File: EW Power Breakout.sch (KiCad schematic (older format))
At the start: 0 parts

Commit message: Jacks and labels
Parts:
- added J1, J2, J4, J5: JACK_2P, symbol JACK_2P
- added J3: CONN_02X08, symbol CONN_02X08
- added J6: CONN_01X14, symbol CONN_01X14
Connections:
- new net +12V: J6.11 (P11)
- new net +5V: J6.13 (P13)
- new net -12V: J6.12 (P12)
- new net CV: J3.4 (P4), J6.10 (P10)
- new net GATE: J3.2 (P2), J6.9 (P9)
- new net GND: J1.3, J2.3, J4.3, J5.3, J6.14 (P14)
- new net J1: J1.1, J6.1 (P1)
- new net J1SW: J1.2, J6.2 (P2)
- new net J2: J2.1, J6.3 (P3)
- new net J2SW: J2.2, J6.4 (P4)
- new net J3: J4.1, J6.5 (P5)
- new net J3SW: J4.2, J6.6 (P6)
- new net J4: J5.1, J6.7 (P7)
- new net J4SW: J5.2, J6.8 (P8)
- no-connect marks 0 -> 1
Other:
- note added: "+12V"
- note added: "-12V"
- note added: "5V (not connected)"
- note added: "GND"
- note added: "SW=switch"
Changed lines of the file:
@@
 Comment4 ""
 $EndDescr
+$Comp
+L CONN_02X08 J3
+U 1 1 599C453D
+P 2900 3150
+F 0 "J3" H 2900 3600 50  0000 C CNN
+F 1 "CONN_02X08" V 2900 3150 50  0000 C CNN
+F 2 "" H 2900 1950 50  0001 C CNN
+F 3 "" H 2900 1950 50  0001 C CNN
+	1    2900 3150
+	1    0    0    -1
+$EndComp
+$Comp
+L CONN_01X14 J6
+U 1 1 599C456D
+P 7700 3250
+F 0 "J6" H 7700 4000 50  0000 C CNN
+F 1 "CONN_01X14" V 7800 3250 50  0000 C CNN
+F 2 "" H 7700 3250 50  0001 C CNN
+F 3 "" H 7700 3250 50  0001 C CNN
+	1    7700 3250
+	1    0    0    -1
+$EndComp
+$Comp
+L JACK_2P J1
+U 1 1 599C45B8
+P 2150 1200
+F 0 "J1" H 1800 1000 50  0000 C CNN
+F 1 "JACK_2P" H 2000 1450 50  0000 C CNN
+F 2 "" H 2150 1200 50  0001 C CNN
+F 3 "" H 2150 1200 50  0001 C CNN
+	1    2150 1200
+	1    0    0    -1
+$EndComp
+$Comp
+L JACK_2P J2
+U 1 1 599C461E
+P 2150 1750
+F 0 "J2" H 1800 1550 50  0000 C CNN
+F 1 "JACK_2P" H 2000 2000 50  0000 C CNN
+F 2 "" H 2150 1750 50  0001 C CNN
+F 3 "" H 2150 1750 50  0001 C CNN
+	1    2150 1750
+	1    0    0    -1
+$EndComp
+$Comp
+L JACK_2P J4
+U 1 1 599C4645
+P 3750 1150
+F 0 "J4" H 3400 950 50  0000 C CNN
+F 1 "JACK_2P" H 3600 1400 50  0000 C CNN
+F 2 "" H 3750 1150 50  0001 C CNN
+F 3 "" H 3750 1150 50  0001 C CNN
+	1    3750 1150
+	-1   0    0    1
+$EndComp
+$Comp
+L JACK_2P J5
+U 1 1 599C4690
+P 3750 1700
+F 0 "J5" H 3400 1500 50  0000 C CNN
+F 1 "JACK_2P" H 3600 1950 50  0000 C CNN
+F 2 "" H 3750 1700 50  0001 C CNN
+F 3 "" H 3750 1700 50  0001 C CNN
+	1    3750 1700
+	-1   0    0    1
+$EndComp
+Wire Wire Line
+	2950 1050 2950 2100
+Wire Wire Line
+	3300 1850 2950 1850
+Connection ~ 2950 1850
+Connection ~ 2950 1600
+Wire Wire Line
+	3300 1300 2950 1300
+Connection ~ 2950 1300
+Wire Wire Line
+	2950 1050 2600 1050
+Wire Wire Line
+	2950 1600 2600 1600
+$Comp
+L GND #PWR01
+U 1 1 599C47FD
+P 2950 2100
+F 0 "#PWR01" H 2950 1850 50  0001 C CNN
+F 1 "GND" H 2950 1950 50  0000 C CNN
+F 2 "" H 2950 2100 50  0001 C CNN
+F 3 "" H 2950 2100 50  0001 C CNN
+	1    2950 2100
+	1    0    0    -1
+$EndComp
+Text Label 7500 2600 2    60   ~ 0
+J1
+Text Label 7500 2700 2    60   ~ 0
+J1SW
+Text Label 2600 1300 0    60   ~ 0
+J1
+Text Label 2600 1200 0    60   ~ 0
+J1SW
+Text Label 7500 2800 2    60   ~ 0
+J2
+Text Label 7500 2900 2    60   ~ 0
+J2SW
+Text Notes 7800 2700 0    60   ~ 0
+SW=switch
+Text Label 7500 3000 2    60   ~ 0
+J3
+Text Label 7500 3100 2    60   ~ 0
+J3SW
+Text Label 7500 3200 2    60   ~ 0
+J4
+Text Label 7500 3300 2    60   ~ 0
+J4SW
+Text Label 7500 3400 2    60   ~ 0
+GATE
+Text Label 7500 3500 2    60   ~ 0
+CV
+Text Label 7500 3600 2    60   ~ 0
++12V
+Text Label 7500 3700 2    60   ~ 0
+-12V
+Text Label 7500 3800 2    60   ~ 0
++5V
+Text Label 7500 3900 2    60   ~ 0
+GND
+Text Label 2600 1850 0    60   ~ 0
+J2
+Text Label 2600 1750 0    60   ~ 0
+J2SW
+Text Label 3300 1050 2    60   ~ 0
+J3
+Text Label 3300 1150 2    60   ~ 0
+J3SW
+Text Label 3300 1600 2    60   ~ 0
+J4
+Text Label 3300 1700 2    60   ~ 0
+J4SW
+Text Label 3150 2800 0    60   ~ 0
+GATE
+Text Label 3150 2900 0    60   ~ 0
+CV
+NoConn ~ 3150 3000
+Text Notes 3150 3000 0    60   ~ 0
+5V (not connected)
+Text Notes 3150 3100 0    60   ~ 0
++12V
+Text Notes 3150 3200 0    60   ~ 0
+GND
+Text Notes 3150 3300 0    60   ~ 0
+GND
+Text Notes 3150 3400 0    60   ~ 0
+GND
+Text Notes 3150 3500 0    60   ~ 0
+-12V
 $EndSCHEMATC

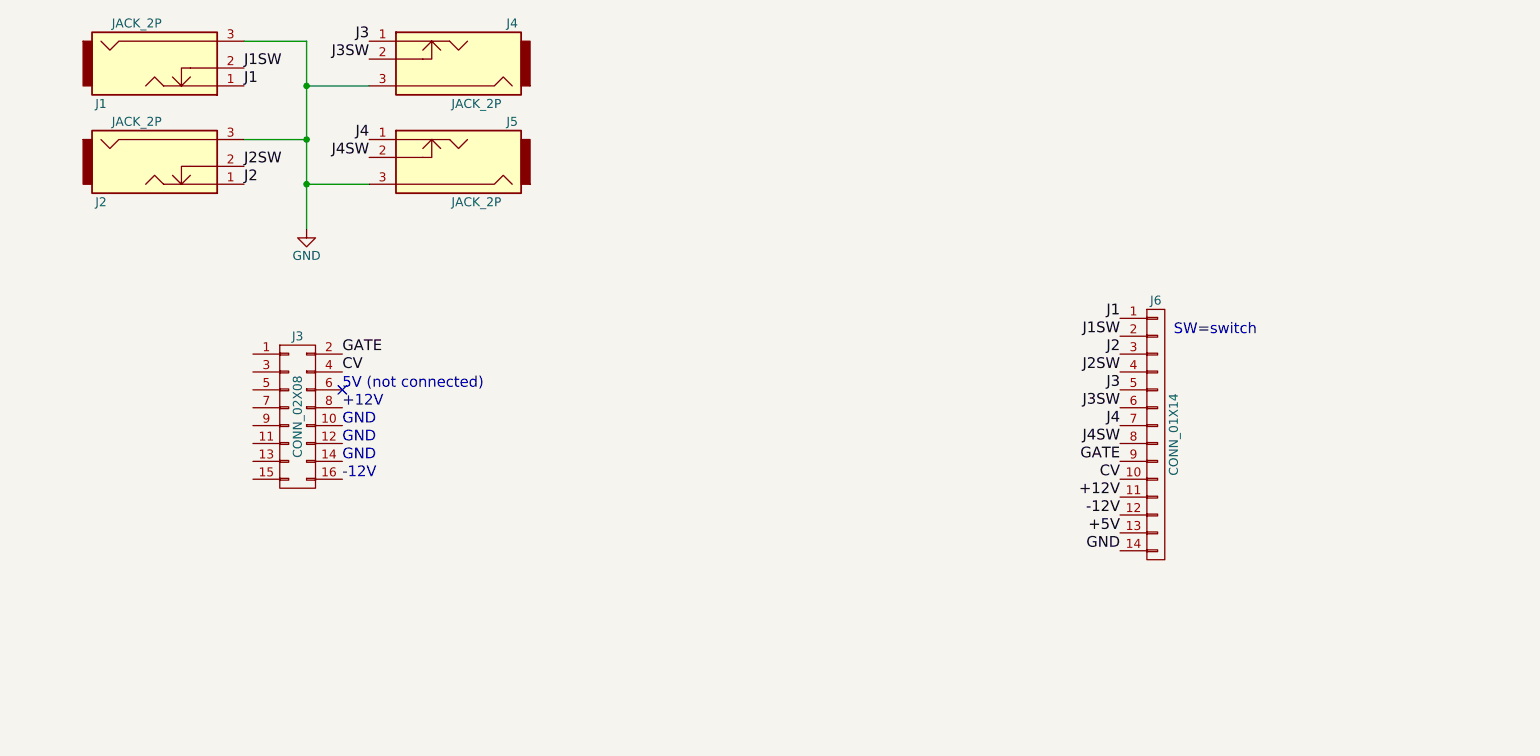
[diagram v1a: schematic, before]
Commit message: Schematic done
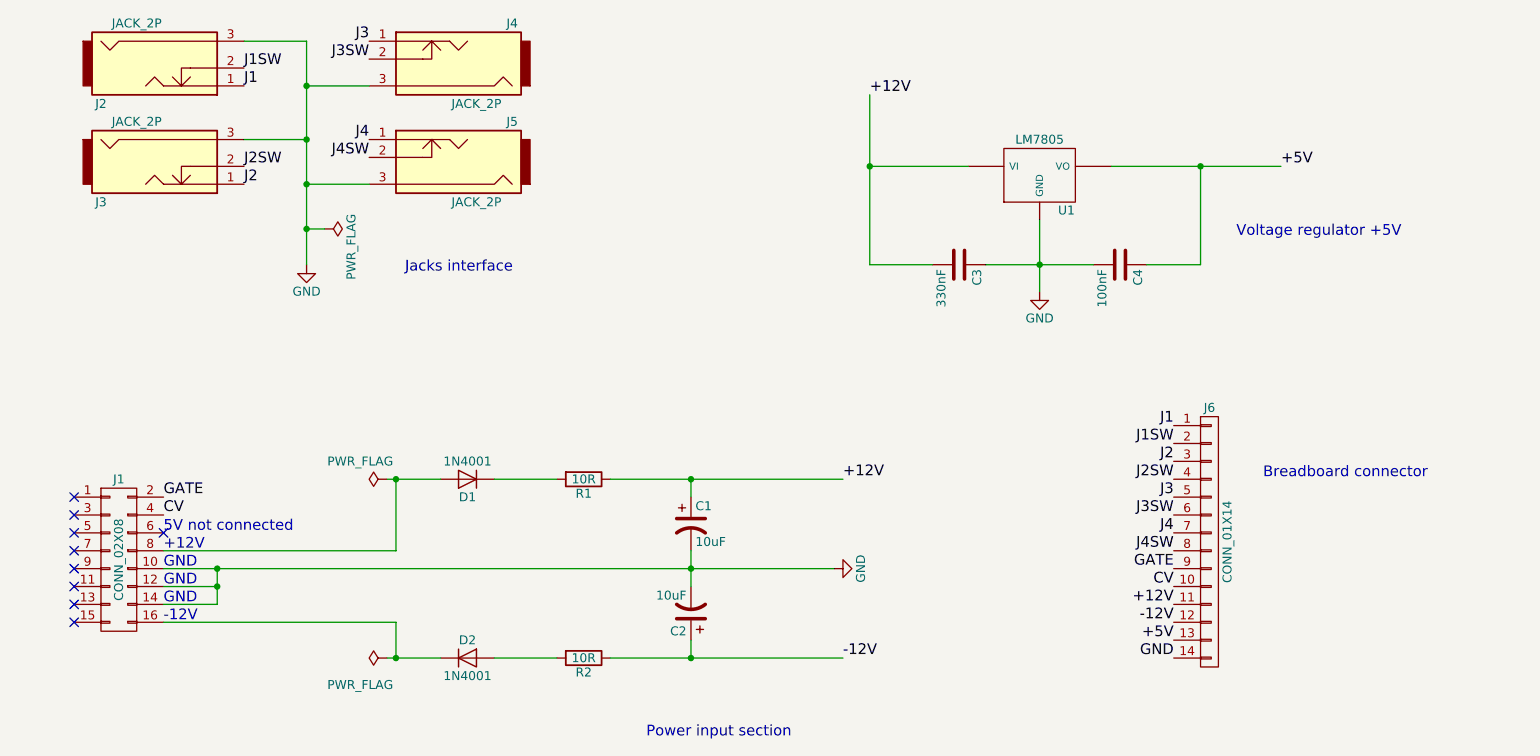
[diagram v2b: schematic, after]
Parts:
- added C1, C2: 10uF, symbol CP1
- added C3: 330nF, symbol C
- added C4: 100nF, symbol C
- added D1, D2: 1N4001, symbol D
- added R1, R2: 10R, symbol R
- added U1: LM7805, symbol LM7805
- renumbered J3 to J1, J1 to J2, J2 to J3
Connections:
- net +12V: now also C1.1, C3.2, R1.1, U1.1 (VI)
- net +5V: now also C4.1, U1.3 (VO)
- net -12V: now also C2.1, R2.1
- net GND: now also J1.10 (P10), J1.12 (P12), J1.14 (P14), C1.2, C2.2, C3.1, C4.2, U1.2 (GND)
- net at J1.16 (P16): now also D2.1 (K)
- net at J1.8 (P8): now also D1.2 (A)
- new net: D1.1 (K), R1.2
- new net: D2.2 (A), R2.2
- no-connect marks 1 -> 9
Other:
- note added: "5V not connected"
- note added: "Breadboard connector"
- note added: "Jacks interface"
- note added: "Power input section"
- note added: "Voltage regulator +5V"
- note removed: "5V (not connected)"
- note removed: "SW=switch"
- moved on the sheet: J1, J6

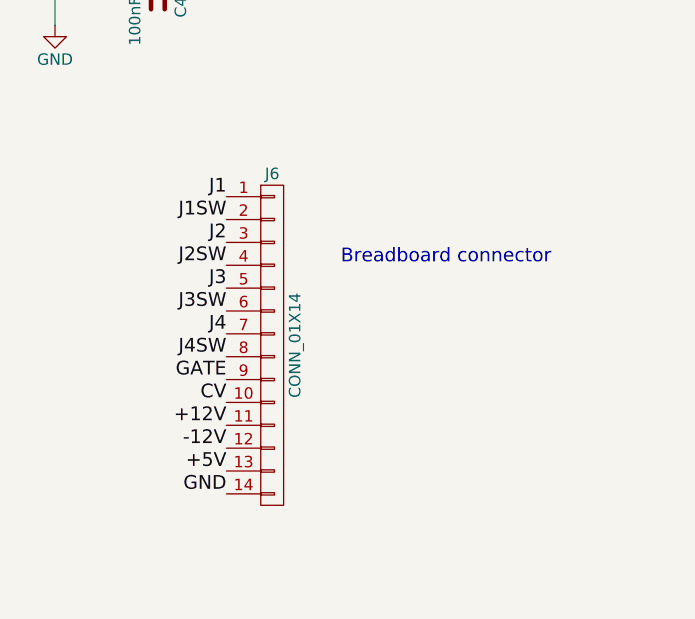
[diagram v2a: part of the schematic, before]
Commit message: Component associations made
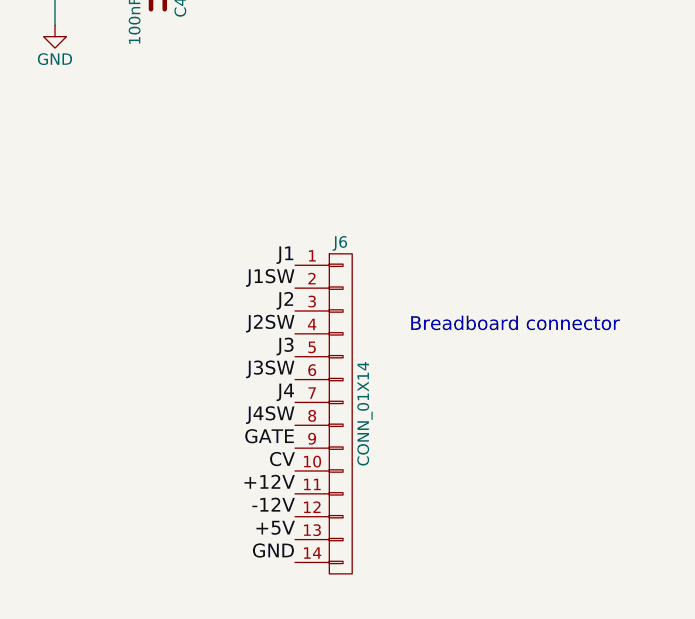
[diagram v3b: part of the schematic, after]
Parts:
- C1, C2: footprint (none) -> Capacitors_THT:CP_Radial_D5.0mm_P2.00mm
- C3, C4: footprint (none) -> Capacitors_THT:C_Disc_D6.0mm_W4.4mm_P5.00mm
- D1, D2: footprint (none) -> Diodes_THT:D_DO-41_SOD81_P12.70mm_Horizontal
- J1: footprint (none) -> Connectors:IDC_Header_Straight_16pins
- J2, J3, J4, J5: footprint (none) -> Eurocad:PJ301M-12
- J6: footprint (none) -> Pin_Headers:Pin_Header_Straight_1x14_Pitch2.54mm
- R1, R2: footprint (none) -> Resistors_THT:R_Axial_DIN0207_L6.3mm_D2.5mm_P10.16mm_Horizontal
- U1: footprint (none) -> TO_SOT_Packages_THT:TO-220_Vertical
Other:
- moved on the sheet: J6
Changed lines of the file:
@@
 LIBS:contrib
 LIBS:valves
+LIBS:EW Power Breakout-cache
 EELAYER 25 0
 EELAYER END
@@
 F 0 "J1" H 1900 4400 50  0000 C CNN
 F 1 "CONN_02X08" V 1900 3950 50  0000 C CNN
-F 2 "" H 1900 2750 50  0001 C CNN
+F 2 "Connectors:IDC_Header_Straight_16pins" H 1900 2750 50  0001 C CNN
 F 3 "" H 1900 2750 50  0001 C CNN
 	1    1900 3950
@@
 L CONN_01X14 J6
 U 1 1 599C456D
-P 8000 3850
-F 0 "J6" H 8000 4600 50  0000 C CNN
-F 1 "CONN_01X14" V 8100 3850 50  0000 C CNN
-F 2 "" H 8000 3850 50  0001 C CNN
-F 3 "" H 8000 3850 50  0001 C CNN
-	1    8000 3850
+P 8300 4150
+F 0 "J6" H 8300 4900 50  0000 C CNN
+F 1 "CONN_01X14" V 8400 4150 50  0000 C CNN
+F 2 "Pin_Headers:Pin_Header_Straight_1x14_Pitch2.54mm" H 8300 4150 50  0001 C CNN
+F 3 "" H 8300 4150 50  0001 C CNN
+	1    8300 4150
 	1    0    0    -1
 $EndComp
@@
 F 0 "J2" H 1800 1000 50  0000 C CNN
 F 1 "JACK_2P" H 2000 1450 50  0000 C CNN
-F 2 "" H 2150 1200 50  0001 C CNN
+F 2 "Eurocad:PJ301M-12" H 2150 1200 50  0001 C CNN
 F 3 "" H 2150 1200 50  0001 C CNN
 	1    2150 1200
@@
 F 0 "J3" H 1800 1550 50  0000 C CNN
 F 1 "JACK_2P" H 2000 2000 50  0000 C CNN
-F 2 "" H 2150 1750 50  0001 C CNN
+F 2 "Eurocad:PJ301M-12" H 2150 1750 50  0001 C CNN
 F 3 "" H 2150 1750 50  0001 C CNN
 	1    2150 1750
@@
 F 0 "J4" H 3400 950 50  0000 C CNN
 F 1 "JACK_2P" H 3600 1400 50  0000 C CNN
-F 2 "" H 3750 1150 50  0001 C CNN
+F 2 "Eurocad:PJ301M-12" H 3750 1150 50  0001 C CNN
 F 3 "" H 3750 1150 50  0001 C CNN
 	1    3750 1150
@@
 F 0 "J5" H 3400 1500 50  0000 C CNN
 F 1 "JACK_2P" H 3600 1950 50  0000 C CNN
-F 2 "" H 3750 1700 50  0001 C CNN
+F 2 "Eurocad:PJ301M-12" H 3750 1700 50  0001 C CNN
 F 3 "" H 3750 1700 50  0001 C CNN
 	1    3750 1700
@@
 $EndComp
 $Comp
-L GND #PWR1
+L GND #PWR01
 U 1 1 599C47FD
 P 2950 2300
-F 0 "#PWR1" H 2950 2050 50  0001 C CNN
+F 0 "#PWR01" H 2950 2050 50  0001 C CNN
 F 1 "GND" H 2950 2150 50  0000 C CNN
 F 2 "" H 2950 2300 50  0001 C CNN
@@
 	1    0    0    -1
 $EndComp
-Text Label 7800 3200 2    60   ~ 0
+Text Label 8100 3500 2    60   ~ 0
 J1
-Text Label 7800 3300 2    60   ~ 0
+Text Label 8100 3600 2    60   ~ 0
 J1SW
 Text Label 2600 1300 0    60   ~ 0
@@
 Text Label 2600 1200 0    60   ~ 0
 J1SW
-Text Label 7800 3400 2    60   ~ 0
+Text Label 8100 3700 2    60   ~ 0
 J2
-Text Label 7800 3500 2    60   ~ 0
+Text Label 8100 3800 2    60   ~ 0
 J2SW
-Text Label 7800 3600 2    60   ~ 0
+Text Label 8100 3900 2    60   ~ 0
 J3
-Text Label 7800 3700 2    60   ~ 0
+Text Label 8100 4000 2    60   ~ 0
 J3SW
-Text Label 7800 3800 2    60   ~ 0
+Text Label 8100 4100 2    60   ~ 0
 J4
-Text Label 7800 3900 2    60   ~ 0
+Text Label 8100 4200 2    60   ~ 0
 J4SW
-Text Label 7800 4000 2    60   ~ 0
+Text Label 8100 4300 2    60   ~ 0
 GATE
-Text Label 7800 4100 2    60   ~ 0
+Text Label 8100 4400 2    60   ~ 0
 CV
-Text Label 7800 4200 2    60   ~ 0
+Text Label 8100 4500 2    60   ~ 0
 +12V
-Text Label 7800 4300 2    60   ~ 0
+Text Label 8100 4600 2    60   ~ 0
 -12V
-Text Label 7800 4400 2    60   ~ 0
+Text Label 8100 4700 2    60   ~ 0
 +5V
-Text Label 7800 4500 2    60   ~ 0
+Text Label 8100 4800 2    60   ~ 0
 GND
 Text Label 2600 1850 0    60   ~ 0
@@
 F 0 "D1" H 3850 3600 50  0000 C CNN
 F 1 "1N4001" H 3850 3400 50  0000 C CNN
-F 2 "" H 3850 3500 50  0001 C CNN
+F 2 "Diodes_THT:D_DO-41_SOD81_P12.70mm_Horizontal" H 3850 3500 50  0001 C CNN
 F 3 "" H 3850 3500 50  0001 C CNN
 	1    3850 3500
@@
 F 0 "D2" H 3850 4600 50  0000 C CNN
 F 1 "1N4001" H 3850 4400 50  0000 C CNN
-F 2 "" H 3850 4500 50  0001 C CNN
+F 2 "Diodes_THT:D_DO-41_SOD81_P12.70mm_Horizontal" H 3850 4500 50  0001 C CNN
 F 3 "" H 3850 4500 50  0001 C CNN
 	1    3850 4500
@@
 F 0 "R1" V 4580 3500 50  0000 C CNN
 F 1 "10R" V 4500 3500 50  0000 C CNN
-F 2 "" V 4430 3500 50  0001 C CNN
+F 2 "Resistors_THT:R_Axial_DIN0207_L6.3mm_D2.5mm_P10.16mm_Horizontal" V 4430 3500 50  0001 C CNN
 F 3 "" H 4500 3500 50  0001 C CNN
 	1    4500 3500
@@
 F 0 "R2" V 4580 4500 50  0000 C CNN
 F 1 "10R" V 4500 4500 50  0000 C CNN
-F 2 "" V 4430 4500 50  0001 C CNN
+F 2 "Resistors_THT:R_Axial_DIN0207_L6.3mm_D2.5mm_P10.16mm_Horizontal" V 4430 4500 50  0001 C CNN
 F 3 "" H 4500 4500 50  0001 C CNN
 	1    4500 4500
@@
 F 0 "C1" H 5125 3850 50  0000 L CNN
 F 1 "10uF" H 5125 3650 50  0000 L CNN
-F 2 "" H 5100 3750 50  0001 C CNN
+F 2 "Capacitors_THT:CP_Radial_D5.0mm_P2.00mm" H 5100 3750 50  0001 C CNN
 F 3 "" H 5100 3750 50  0001 C CNN
 	1    5100 3750
@@
 F 0 "C2" H 5125 4350 50  0000 L CNN
 F 1 "10uF" H 5125 4150 50  0000 L CNN
-F 2 "" H 5100 4250 50  0001 C CNN
+F 2 "Capacitors_THT:CP_Radial_D5.0mm_P2.00mm" H 5100 4250 50  0001 C CNN
 F 3 "" H 5100 4250 50  0001 C CNN
 	1    5100 4250
@@
 $EndComp
 $Comp
-L GND #PWR2
+L GND #PWR02
 U 1 1 599C5139
 P 5900 4000
-F 0 "#PWR2" H 5900 3750 50  0001 C CNN
+F 0 "#PWR02" H 5900 3750 50  0001 C CNN
 F 1 "GND" H 5900 3850 50  0000 C CNN
 F 2 "" H 5900 4000 50  0001 C CNN
@@
 -12V
 $Comp
-L PWR_FLAG #FLG1
+L PWR_FLAG #FLG03
 U 1 1 599C57EA
 P 3050 2100
-F 0 "#FLG1" H 3050 2175 50  0001 C CNN
+F 0 "#FLG03" H 3050 2175 50  0001 C CNN
 F 1 "PWR_FLAG" H 3150 2250 50  0000 C CNN
 F 2 "" H 3050 2100 50  0001 C CNN
@@
 $EndComp
 $Comp
-L PWR_FLAG #FLG2
+L PWR_FLAG #FLG04
 U 1 1 599C5844
 P 3400 3500
-F 0 "#FLG2" H 3400 3575 50  0001 C CNN
+F 0 "#FLG04" H 3400 3575 50  0001 C CNN
 F 1 "PWR_FLAG" V 3500 3650 50  0000 C CNN
 F 2 "" H 3400 3500 50  0001 C CNN
@@
 $EndComp
 $Comp
-L PWR_FLAG #FLG3
+L PWR_FLAG #FLG05
 U 1 1 599C5897
 P 3400 4500
-F 0 "#FLG3" H 3400 4575 50  0001 C CNN
+F 0 "#FLG05" H 3400 4575 50  0001 C CNN
 F 1 "PWR_FLAG" V 3250 4650 50  0000 C CNN
 F 2 "" H 3400 4500 50  0001 C CNN
@@
 F 0 "U1" H 7200 1604 50  0000 C CNN
 F 1 "LM7805" H 7050 2000 50  0000 C CNN
-F 2 "" H 7050 1800 50  0001 C CNN
+F 2 "TO_SOT_Packages_THT:TO-220_Vertical" H 7050 1800 50  0001 C CNN
 F 3 "" H 7050 1800 50  0001 C CNN
 	1    7050 1800
@@
 $EndComp
 $Comp
-L GND #PWR3
+L GND #PWR06
 U 1 1 599C5CBD
 P 7050 2450
-F 0 "#PWR3" H 7050 2200 50  0001 C CNN
+F 0 "#PWR06" H 7050 2200 50  0001 C CNN
 F 1 "GND" H 7050 2300 50  0000 C CNN
 F 2 "" H 7050 2450 50  0001 C CNN
@@
 F 0 "C3" H 6625 2400 50  0000 L CNN
 F 1 "330nF" H 6625 2200 50  0000 L CNN
-F 2 "" H 6638 2150 50  0001 C CNN
+F 2 "Capacitors_THT:C_Disc_D6.0mm_W4.4mm_P5.00mm" H 6638 2150 50  0001 C CNN
 F 3 "" H 6600 2300 50  0001 C CNN
 	1    6600 2300
@@
 F 0 "C4" H 7525 2400 50  0000 L CNN
 F 1 "100nF" H 7525 2200 50  0000 L CNN
-F 2 "" H 7538 2150 50  0001 C CNN
+F 2 "Capacitors_THT:C_Disc_D6.0mm_W4.4mm_P5.00mm" H 7538 2150 50  0001 C CNN
 F 3 "" H 7500 2300 50  0001 C CNN
 	1    7500 2300
@@
 Wire Wire Line
 	6450 2300 6100 2300
-Text Notes 8300 3500 0    60   ~ 0
+Text Notes 8600 3800 0    60   ~ 0
 Breadboard connector
 Text Notes 3500 2350 0    60   ~ 0
